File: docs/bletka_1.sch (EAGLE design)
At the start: 19 parts

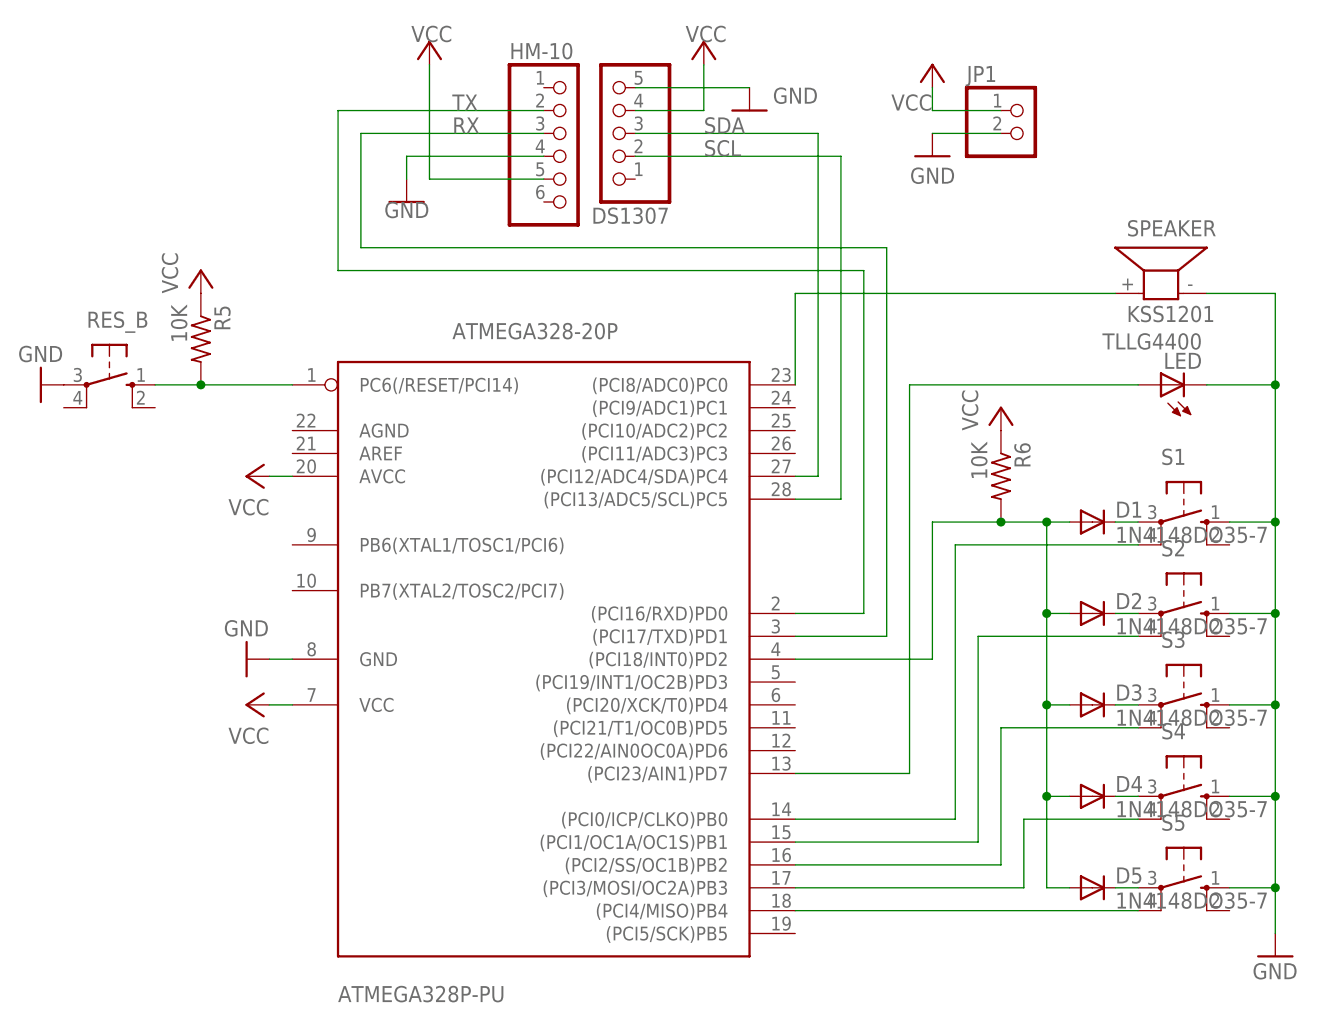
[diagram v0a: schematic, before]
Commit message: [FEATURE] Schematic Diagram & Board
 - adds images of BLETKA with 1 button to readme
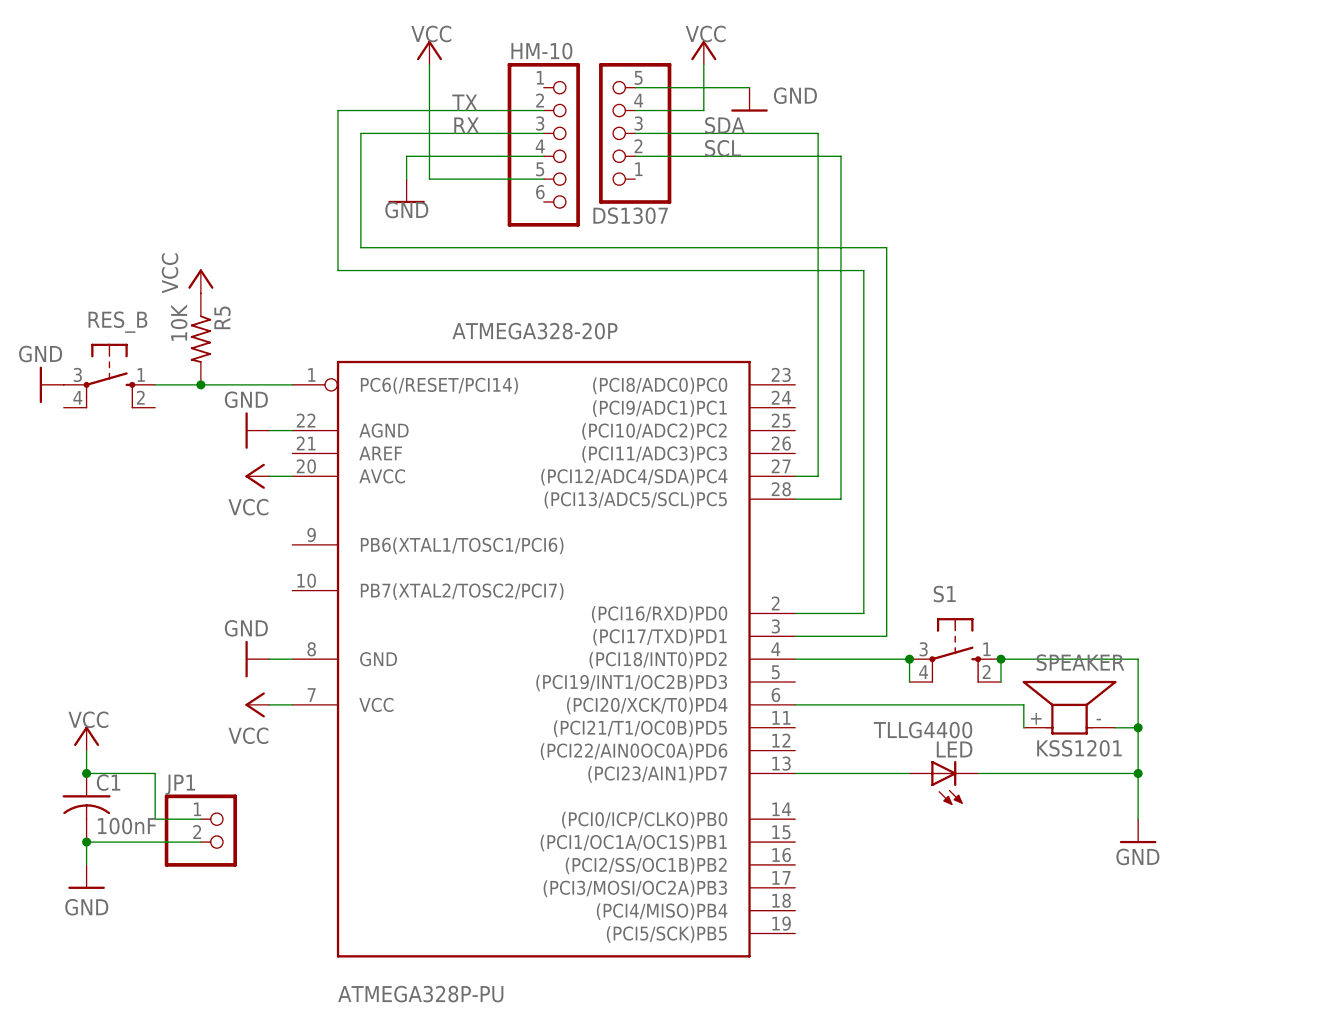
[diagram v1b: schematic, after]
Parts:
- removed D1, D2, D3, D4, D5: 1N4148DO35-7, diode:1N4148DO35-7
- removed R6: 10K, adafruit:R-US_0207/10
- removed S2, S3, S4, S5: (no value), switch-omron:10-XX
- added C1: 100nF, adafruit:C-US050-024X044
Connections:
- removed net INT0: ATMEGA328P-PU.(PCI18/INT0)PD2, D1.A, D2.A, D3.A, D4.A, D5.A, R6.2
- removed net N$10: D4.C, S4.P
- removed net N$6: D1.C, S1.P
- removed net N$7: D5.C, S5.P
- removed net N$8: D2.C, S2.P
- removed net N$9: D3.C, S3.P
- removed net PB0: ATMEGA328P-PU.(PCI0/ICP/CLKO)PB0, S1.P1
- removed net PB1: ATMEGA328P-PU.(PCI1/OC1A/OC1S)PB1, S2.P1
- removed net PB2: ATMEGA328P-PU.(PCI2/SS/OC1B)PB2, S3.P1
- removed net PB3: ATMEGA328P-PU.(PCI3/MOSI/OC2A)PB3, S4.P1
- removed net PB4: ATMEGA328P-PU.(PCI4/MISO)PB4, S5.P1
- removed net PC0: ATMEGA328P-PU.(PCI8/ADC0)PC0, SPEAKER.1
- new net N$1: ATMEGA328P-PU.(PCI18/INT0)PD2, S1.P, S1.P1
- new net PD4: ATMEGA328P-PU.(PCI20/XCK/T0)PD4, SPEAKER.1
- net GND: now also ATMEGA328P-PU.AGND, C1.2, S1.S1; no longer S2.S, S3.S, S4.S, S5.S
- net VCC: now also C1.1; no longer R6.1
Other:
- moved on the sheet: JP1, LED, S1, SPEAKER
